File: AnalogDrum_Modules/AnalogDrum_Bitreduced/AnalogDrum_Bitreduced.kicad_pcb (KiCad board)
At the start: 2 copper layers, 100.3 x 160 mm, 147 parts, among them J101 Conn_01x05_Male, Q301 2N3904, Q302 2N3904, Q303 2N3904, Q401 2N3904, Q402 2N3904, Q601 J112, SW201 SW_DPDT_x2, SW202 SW_DPDT_x2, U201 TL074, U301 TL074, U302 LM358, U401 NE5532, U501 LM13700, U502 NE5532, U601 NE5532, U602 NE5532, U701 NE5532, U702 NE5532

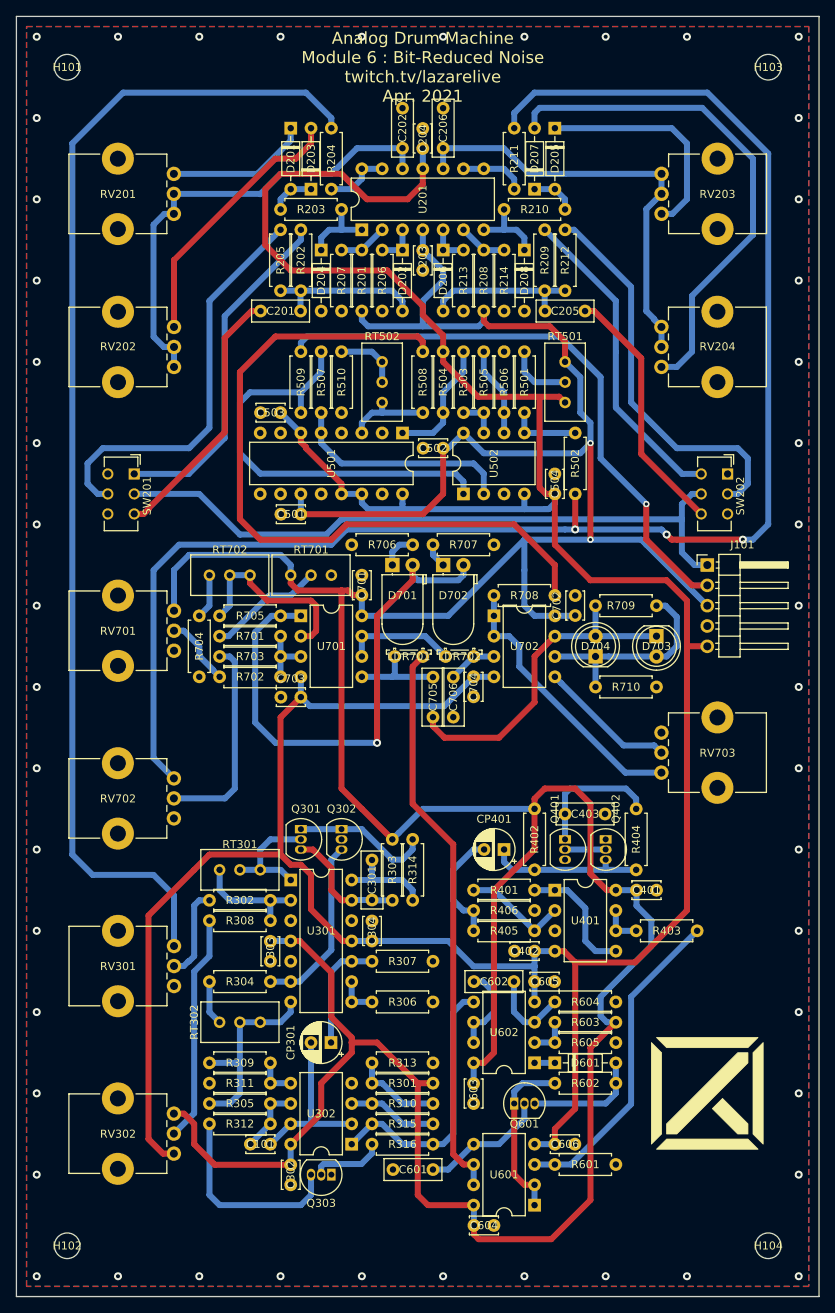
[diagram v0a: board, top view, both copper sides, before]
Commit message: Version 0.1.1
Corrections mineures :
- Vérification des potentiomètres
- Passage des connecteurs de carte e n JST
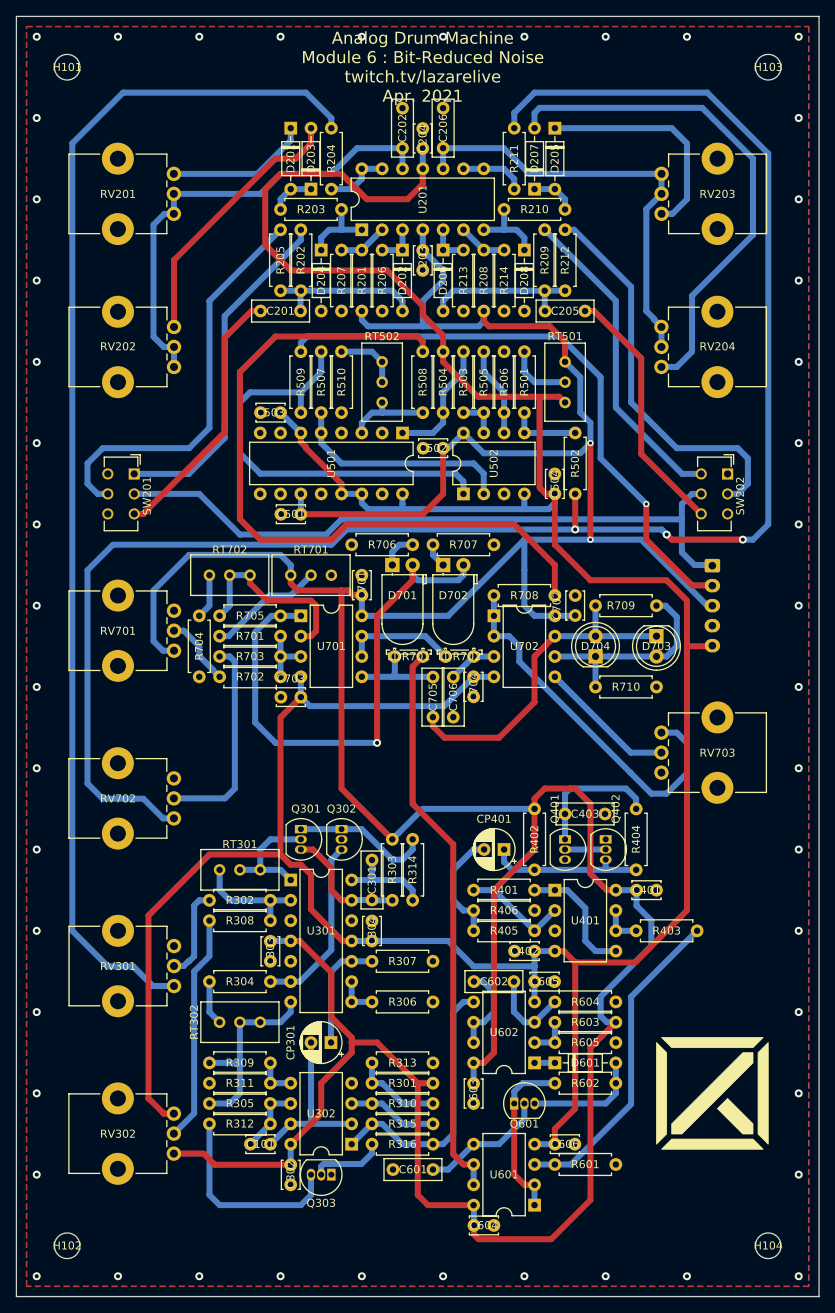
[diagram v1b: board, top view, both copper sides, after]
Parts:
- J101: footprint Connector_PinHeader_2.54mm:PinHeader_1x05_P2.54mm_Horizontal -> Connector_JST:JST_EH_B5B-EH-A_1x05_P2.50mm_Vertical; moved to B.Cu
- moved J101 0.64 mm to (151.8, 96.6), turned to 270 degrees
- moved REF** 0.63 mm to (151.8, 162.6)
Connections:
- RV301 pad 1: /EG/EGA_OUT -> GNDA
- RV301 pad 3: GNDA -> /EG/EGA_OUT
- RV302 pad 1: +12V -> -12V
- RV302 pad 3: -12V -> +12V
- RV701 pad 1: +12V -> GNDA
- RV701 pad 3: GNDA -> +12V
- RV702 pad 1: /EG/EGB_OUT -> GNDA
- RV702 pad 3: GNDA -> /EG/EGB_OUT
- RV703 pad 1: Net-(R708-Pad2) -> GNDA
- RV703 pad 3: GNDA -> Net-(R708-Pad2)
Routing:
- net /EG/EGB_OUT: track 196.0 -> 216.4 mm
- net Net-(R708-Pad2): track 34.6 -> 47.1 mm
- net -12V: track 405.4 -> 400.4 mm
- net +12V: track 491.6 -> 496.0 mm
- net /EG/EGA_OUT: track 147.7 -> 151.6 mm
